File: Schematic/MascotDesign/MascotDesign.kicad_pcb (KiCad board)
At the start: 2 copper layers, 64 x 35.6 mm, 41 parts, among them J1 Charger input, J10 AudioJack4, J11 Main power cutoff (soldered s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, J2 PI power USB, J3 LCD LED Power, J5 Audio in, J6 Audio in, J8 Potentiometer, J9 Speaker 8R, U1 Generic_Buck_Regulator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

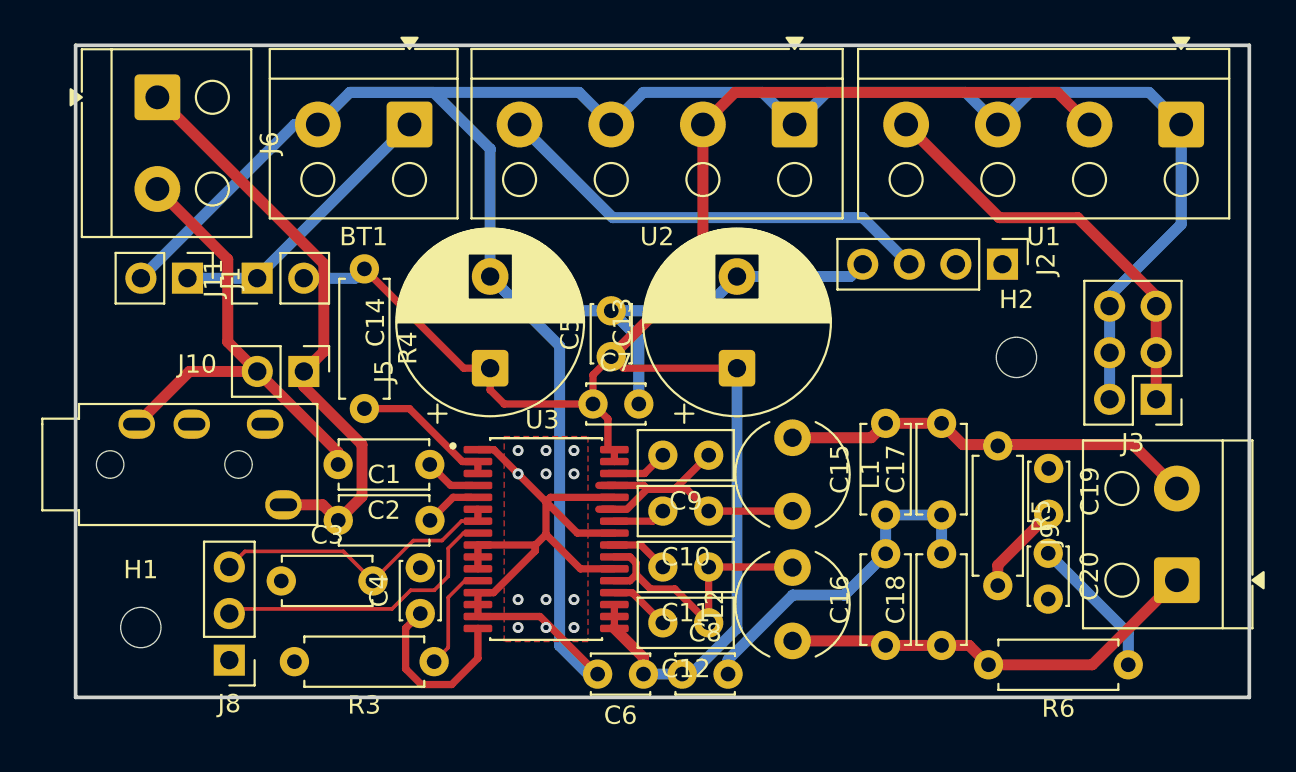
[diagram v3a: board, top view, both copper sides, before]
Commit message: ensure board passes DRC errors
not warnings though. Those are mostly just silkscreen overlaps.
We need to put something funny on the silkscreen yet.
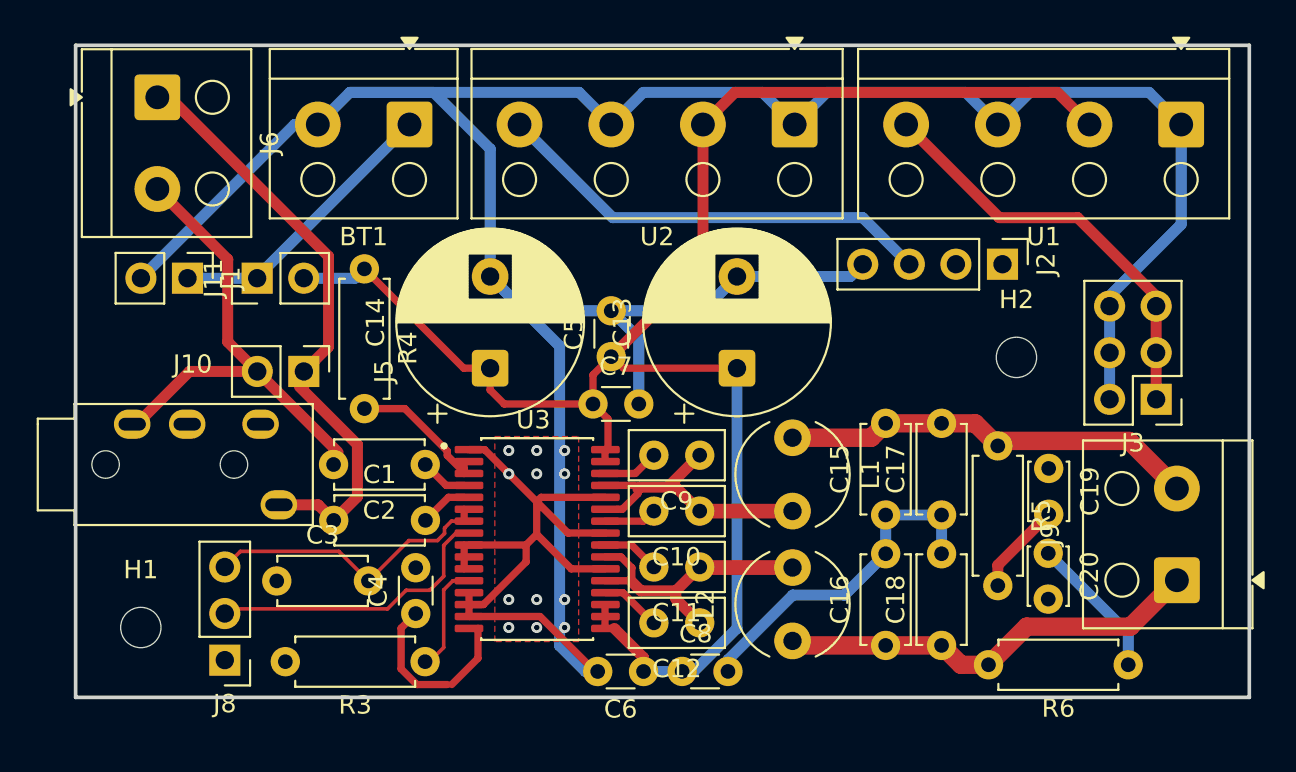
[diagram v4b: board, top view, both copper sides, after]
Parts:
- C4, C5, C6, C7, C8: footprint Capacitor_THT:C_Disc_D3.0mm_W2.0mm_P2.50mm -> Capacitor_THT:C_Disc_D3.0mm_W1.6mm_P2.50mm
- moved R3 0.49 mm to (96.3, 95.3)
- moved C10 0.49 mm to (111.3, 87.1)
- moved C11 0.49 mm to (111.3, 90.2)
- moved C12 0.49 mm to (111.3, 93.2)
- moved C9 0.49 mm to (111.3, 84.1)
- moved U3 0.49 mm to (102.4, 88.6)
- moved C1 0.25 mm to (91.3, 87.6)
- moved C2 0.25 mm to (96.3, 84.6)
- moved C3 0.25 mm to (88.2, 90.9)
- moved C4 0.25 mm to (95.8, 92.7)
- moved J10 0.25 mm to (75.2, 82.4)
- moved J8 0.25 mm to (85.4, 95.2)
- moved C8 0.15 mm to (110.3, 95.9)
- moved C6 0.14 mm to (108.2, 95.9)
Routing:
- net Net-(U3-OUTNR): track 18.0 -> 15.5 mm
- net GND: track 208.0 -> 209.0 mm
- net Net-(J5-Pin_1): track 32.5 -> 33.1 mm

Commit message: Tweak PCB and make power traces slightly thicker
They should be plenty wide for our application, but if we have room, we may as well.
I may go back and replace the speaker output traces with fill zones later to minimize impedance.
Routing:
- net 12V SWITCHED: track 95.1 -> 117.5 mm
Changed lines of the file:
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@@
 		(tags "Resistor Axial_DIN0207 series Axial Horizontal pin pitch 7.62mm 0.25W = 1/4W length 6.3mm diameter 2.5mm")
 		(property "Reference" "R4"
-			(at 4.318 -2.37 90)
+			(at 3.81 0 90)
 			(layer "F.SilkS")
 			(effects
@@
 		(tags "Inductor Radial series Radial pin pitch 4.00mm  diameter 6.0mm height 4.6mm")
 		(property "Reference" "L2"
-			(at 2 -4.758 90)
+			(at 2 0 90)
 			(layer "F.SilkS")
 			(effects
@@
 		(at 75.152 82.382)
 		(property "Reference" "J10"
-			(at 8.4455 -3.269 0)
+			(at 7.144 2.454 0)
 			(layer "F.SilkS")
 			(effects
@@
 		(tags "CP Radial series Radial pin pitch 5.00mm diameter 10mm height 16mm Electrolytic Capacitor")
 		(property "Reference" "C13"
-			(at 2.5 -6.25 90)
+			(at 1.605677 0 180)
 			(layer "F.SilkS")
 			(effects
@@
 		(tags "C Disc series Radial pin pitch 5.00mm diameter 4.7mm width 2.5mm Capacitor")
 		(property "Reference" "C17"
-			(at 2.5 -2.5 90)
+			(at 2.5 0 90)
 			(layer "F.SilkS")
 			(effects
@@
 		(tags "THT terminal block RND 205-00003 pitch 5mm size 20x9mm drill 1.3mm pad 2.5mm")
 		(property "Reference" "U1"
-			(at 7.5 -6.12 0)
+			(at 7.5 0 0)
 			(layer "F.SilkS")
 			(effects
@@
 		(tags "Through hole pin header THT 1x04 2.54mm single row")
 		(property "Reference" "J2"
-			(at 0 -2.38 90)
+			(at 0 -3.048 180)
 			(layer "F.SilkS")
 			(effects
@@
 		(tags "C Disc series Radial pin pitch 2.50mm diameter 3mm width 2mm Capacitor")
 		(property "Reference" "C20"
-			(at 1.25 -2.25 270)
+			(at 1.25 0 180)
 			(layer "F.SilkS")
 			(effects
@@
 		(tags "C Disc series Radial pin pitch 2.50mm diameter 3.0mm width 1.6mm Capacitor")
 		(property "Reference" "C4"
-			(at 1.25 -2.05 90)
+			(at 1.25 0 180)
 			(layer "F.SilkS")
 			(effects
@@
 		(tags "THT terminal block RND 205-00001 pitch 5mm size 10x9mm drill 1.3mm pad 2.5mm")
 		(property "Reference" "BT1"
-			(at 2.5 -6.12 0)
+			(at 2.5 -3.048 0)
 			(layer "F.SilkS")
 			(effects
@@
 		(tags "Resistor Axial_DIN0207 series Axial Horizontal pin pitch 7.62mm 0.25W = 1/4W length 6.3mm diameter 2.5mm")
 		(property "Reference" "R5"
-			(at 3.81 -2.37 90)
+			(at 3.81 0 90)
 			(layer "F.SilkS")
 			(effects
@@
 		(tags "C Disc series Radial pin pitch 5.00mm diameter 4.7mm width 2.5mm Capacitor")
 		(property "Reference" "C1"
-			(at 2.5 -2.5 0)
+			(at 2.5 0 0)
 			(layer "F.SilkS")
 			(effects
@@
 		(tags "Inductor Radial series Radial pin pitch 4.00mm  diameter 6.0mm height 4.6mm")
 		(property "Reference" "L1"
-			(at 2 -4.25 90)
+			(at 2 0 90)
 			(layer "F.SilkS")
 			(effects
@@
 		(tags "C Disc series Radial pin pitch 5.00mm diameter 4.7mm width 2.5mm Capacitor")
 		(property "Reference" "C3"
-			(at 2.5 -2.5 0)
+			(at 2.5 0 0)
 			(layer "F.SilkS")
 			(effects
@@
 		(tags "Resistor Axial_DIN0207 series Axial Horizontal pin pitch 7.62mm 0.25W = 1/4W length 6.3mm diameter 2.5mm")
 		(property "Reference" "R6"
-			(at 3.81 -2.37 0)
+			(at 3.81 0 0)
 			(layer "F.SilkS")
 			(effects
@@
 		)
 		(property "Value" "13.2 R"
-			(at 3.81 2.37 0)
+			(at 3.81 0 0)
 			(layer "F.Fab")
 			(effects
@@
 		(tags "C Disc series Radial pin pitch 2.50mm diameter 3.0mm width 1.6mm Capacitor")
 		(property "Reference" "C7"
-			(at 1.25 -2.05 0)
+			(at 1.25 0 90)
 			(layer "F.SilkS")
 			(effects
@@
 		(tags "C Disc series Radial pin pitch 2.50mm diameter 3.0mm width 1.6mm Capacitor")
 		(property "Reference" "C6"
-			(at 1.25 -2.05 180)
+			(at 4.555688 0 180)
 			(layer "F.SilkS")
 			(effects
@@
 		(tags "C Disc series Radial pin pitch 2.50mm diameter 3.0mm width 1.6mm Capacitor")
 		(property "Reference" "C5"
-			(at 1.25 -2.05 90)
+			(at 1.25 0 0)
 			(layer "F.SilkS")
 			(effects
@@
 		(tags "mountinghole M2")
 		(property "Reference" "H2"
-			(at 0 -3.15 0)
+			(at -3.556 0 0)
 			(layer "F.SilkS")
 			(effects
@@
 		(tags "C Disc series Radial pin pitch 2.50mm diameter 5mm width 2.5mm Capacitor")
 		(property "Reference" "C11"
-			(at 1.27 -2.5 180)
+			(at 1.25 0 270)
 			(layer "F.SilkS")
 			(effects
@@
 		(tags "Through hole pin header THT 1x03 2.54mm single row")
 		(property "Reference" "J8"
-			(at 0 -2.38 0)
+			(at 2.293 -0.762 0)
 			(layer "F.SilkS")
 			(effects
@@
 		(tags "Resistor Axial_DIN0207 series Axial Horizontal pin pitch 7.62mm 0.25W = 1/4W length 6.3mm diameter 2.5mm")
 		(property "Reference" "R3"
-			(at 3.81 -2.37 0)
+			(at 3.81 0 0)
 			(layer "F.SilkS")
 			(effects
@@
 		(tags "Through hole pin header THT 1x02 2.54mm single row")
 		(property "Reference" "J5"
-			(at 0 -4.372 90)
+			(at -0.005 5.08 180)
 			(layer "F.SilkS")
 			(effects
@@
 		(tags "C Disc series Radial pin pitch 2.50mm diameter 5mm width 2.5mm Capacitor")
 		(property "Reference" "C10"
-			(at 1.27 -2.5 180)
+			(at 1.25 0 270)
 			(layer "F.SilkS")
 			(effects
@@
 		(tags "C Disc series Radial pin pitch 5.00mm diameter 4.7mm width 2.5mm Capacitor")
 		(property "Reference" "C15"
-			(at 2.5 -2.5 90)
+			(at 2.5 0 90)
 			(layer "F.SilkS")
 			(effects
@@
 		(tags "THT terminal block RND 205-00003 pitch 5mm size 20x9mm drill 1.3mm pad 2.5mm")
 		(property "Reference" "U2"
-			(at 7.5 -6.12 0)
+			(at 7.5 0 0)
 			(layer "F.SilkS")
 			(effects
@@
 		(tags "CP Radial series Radial pin pitch 5.00mm diameter 10mm height 16mm Electrolytic Capacitor")
 		(property "Reference" "C14"
-			(at 2.5 -6.25 90)
+			(at 1.605677 0 180)
 			(layer "F.SilkS")
 			(effects
@@
 		(tags "Through hole pin header THT 1x02 2.54mm single row")
 		(property "Reference" "J11"
-			(at 0 -2.38 90)
+			(at -2.032 1.021 180)
 			(layer "F.SilkS")
 			(effects
@@
 		(tags "Through hole pin header THT 2x03 2.54mm double row")
 		(property "Reference" "J3"
-			(at 1.27 -2.38 0)
+			(at -2.794 0 90)
 			(layer "F.SilkS")
 			(effects
@@
 		(tags "C Disc series Radial pin pitch 2.50mm diameter 3mm width 2mm Capacitor")
 		(property "Reference" "C19"
-			(at 1.25 -2.25 270)
+			(at -2.499928 -0.019748 270)
 			(layer "F.SilkS")
 			(effects
@@
 		(tags "THT terminal block RND 205-00001 pitch 5mm size 10x9mm drill 1.3mm pad 2.5mm")
 		(property "Reference" "J9"
-			(at 2.5 -6.902 90)
+			(at 2.5 0.1405 180)
 			(layer "F.SilkS")
 			(effects
@@
 		(tags "C Disc series Radial pin pitch 2.50mm diameter 5mm width 2.5mm Capacitor")
 		(property "Reference" "C12"
-			(at 1.25 -2.5 180)
+			(at 1.25 0 270)
 			(layer "F.SilkS")
 			(effects
@@
 		)
 		(property "Value" "1 uF"
-			(at 2.5 2.5 90)
+			(at 2.5 1.036 90)
 			(layer "F.Fab")
 			(effects
@@
 		(tags "C Disc series Radial pin pitch 5.00mm diameter 4.7mm width 2.5mm Capacitor")
 		(property "Reference" "C2"
-			(at 2.5 -2.5 180)
+			(at 2.490445 0 180)
 			(layer "F.SilkS")
 			(effects
@@
 		(tags "Through hole pin header THT 1x02 2.54mm single row")
 		(property "Reference" "J1"
-			(at 0 -2.38 90)
+			(at 2.54 1.275 180)
 			(layer "F.SilkS")
 			(effects
@@
 		(tags "THT terminal block RND 205-00001 pitch 5mm size 10x9mm drill 1.3mm pad 2.5mm")
 		(property "Reference" "J6"
-			(at 2.5 -6.12 90)
+			(at 2.5 0.1405 0)
 			(layer "F.SilkS")
 			(effects
@@
 		(tags "C Disc series Radial pin pitch 2.50mm diameter 5mm width 2.5mm Capacitor")
 		(property "Reference" "C9"
-			(at 1.27 -2.5 180)
+			(at 1.25 0 270)
 			(layer "F.SilkS")
 			(effects
@@
 		(tags "C Disc series Radial pin pitch 2.50mm diameter 3.0mm width 1.6mm Capacitor")
 		(property "Reference" "C8"
-			(at 0.742 -2.05 0)
+			(at 4.516389 0 0)
 			(layer "F.SilkS")
 			(effects
@@
 	)
 	(segment
+		(start 132.508 65.706)
+		(end 132.508 66.04)
+		(width 1)
+		(layer "F.Cu")
+		(net 5)
+	)
+	(segment
 		(start 105.43 81.28)
 		(end 105.43 79.696)
@@
 	)
 	(segment
+		(start 130.556 63.754)
+		(end 132.508 65.706)
+		(width 1)
+		(layer "F.Cu")
+		(net 5)
+	)
+	(segment
+		(start 109.475 67.991)
+		(end 98.887 67.991)
+		(width 1)
+		(layer "F.Cu")
+		(net 5)
+	)
+	(segment
 		(start 108.184 95.109)
 		(end 106.596 93.521)
@@
 	)
 	(segment
+		(start 98.887 67.991)
+		(end 92.964 73.914)
+		(width 1)
+		(layer "F.Cu")
+		(net 5)
+	)
+	(segment
 		(start 105.43 79.696)
 		(end 106.426 78.7)
@@
 	)
 	(segment
+		(start 111.426 66.04)
+		(end 109.475 67.991)
+		(width 1)
+		(layer "F.Cu")
+		(net 5)
+	)
+	(segment
 		(start 111.426 73.7)
 		(end 106.426 78.7)
@@
 	)
 	(segment
-		(start 106.088 93.521)
-		(end 106.088 92.221)
-		(width 0.4)
-		(layer "F.Cu")
-		(net 5)
-	)
-	(segment
-		(start 130.757 64.289)
-		(end 132.508 66.04)
-		(width 0.6)
+		(start 111.426 66.04)
+		(end 113.712 63.754)
+		(width 1)
 		(layer "F.Cu")
 		(net 5)
 	)
 	(segment
-		(start 113.177 64.289)
-		(end 130.757 64.289)
-		(width 0.6)
+		(start 106.088 93.521)
+		(end 106.088 92.221)
+		(width 0.4)
 		(layer "F.Cu")
 		(net 5)
@@
 	)
 	(segment
-		(start 111.426 66.04)
-		(end 113.177 64.289)
-		(width 0.6)
+		(start 113.712 63.754)
+		(end 130.556 63.754)
+		(width 1)
 		(layer "F.Cu")
 		(net 5)
@@
 		(start 92.456 74.422)
 		(end 92.964 73.914)
-		(width 0.6)
+		(width 1)
 		(layer "B.Cu")
 		(net 5)
@@
 		(start 89.657 74.422)
 		(end 92.456 74.422)
-		(width 0.6)
+		(width 1)
 		(layer "B.Cu")
 		(net 5)
@@
 		(start 95.424 66.04)
 		(end 87.117 74.347)
-		(width 0.6)
+		(width 1)
 		(layer "B.Cu")
 		(net 18)
@@
 		(start 86.863 74.422)
 		(end 83.317 74.422)
-		(width 0.6)
+		(width 1)
 		(layer "B.Cu")
 		(net 18)
@@
 		(start 87.117 74.347)
 		(end 87.117 74.422)
-		(width 0.6)
+		(width 1)
 		(layer "B.Cu")
 		(net 18)
@@
 			)
 		)
+	)
+	(zone
+		(net 0)
+		(net_name "")
+		(layer "F.Mask")
+		(hatch edge 0.5)
+		(connect_pads
+			(clearance 0.5)
+		)
+		(min_thickness 0.25)
+		(filled_areas_thickness no)
+		(fill yes
+			(thermal_gap 0.5)
+			(thermal_bridge_width 0.5)
+		)
+		(polygon
+			(pts
+				(xy 104.648 83.058) (xy 100.076 83.058) (xy 100.076 94.234) (xy 104.648 94.234)
+			)
+		)

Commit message: Add screen mounts to CAD and PCB silkscreen
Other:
- board text added: "JLCJLCJLCJLC"
- board text added: "Mascot Head Terminal board Rev. 1.0"

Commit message: Slight PCB tweaking
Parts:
- J1: footprint Connector_PinHeader_2.54mm:PinHeader_1x02_P2.54mm_Vertical -> Connector_JST:JST_XH_B2B-XH-A_1x02_P2.50mm_Vertical
- J3: footprint Connector_PinHeader_2.54mm:PinHeader_2x03_P2.54mm_Vertical -> Connector_PinHeader_2.54mm:PinHeader_2x04_P2.54mm_Vertical
- moved J3 7.65 mm to (135.2, 73.4), turned to 0 degrees
- moved J1 4.51 mm to (80.8, 78.2), turned to 90 degrees
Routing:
- net +12V: track 15.4 -> 19.5 mm
- net Net-(J9-Pin_2): track 23.0 -> 24.3 mm
- net GND: track 209.0 -> 208.0 mm, vias 12 -> 18
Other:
- board text added: "github.com/DrGlaucous/mascot-head-sr-design"

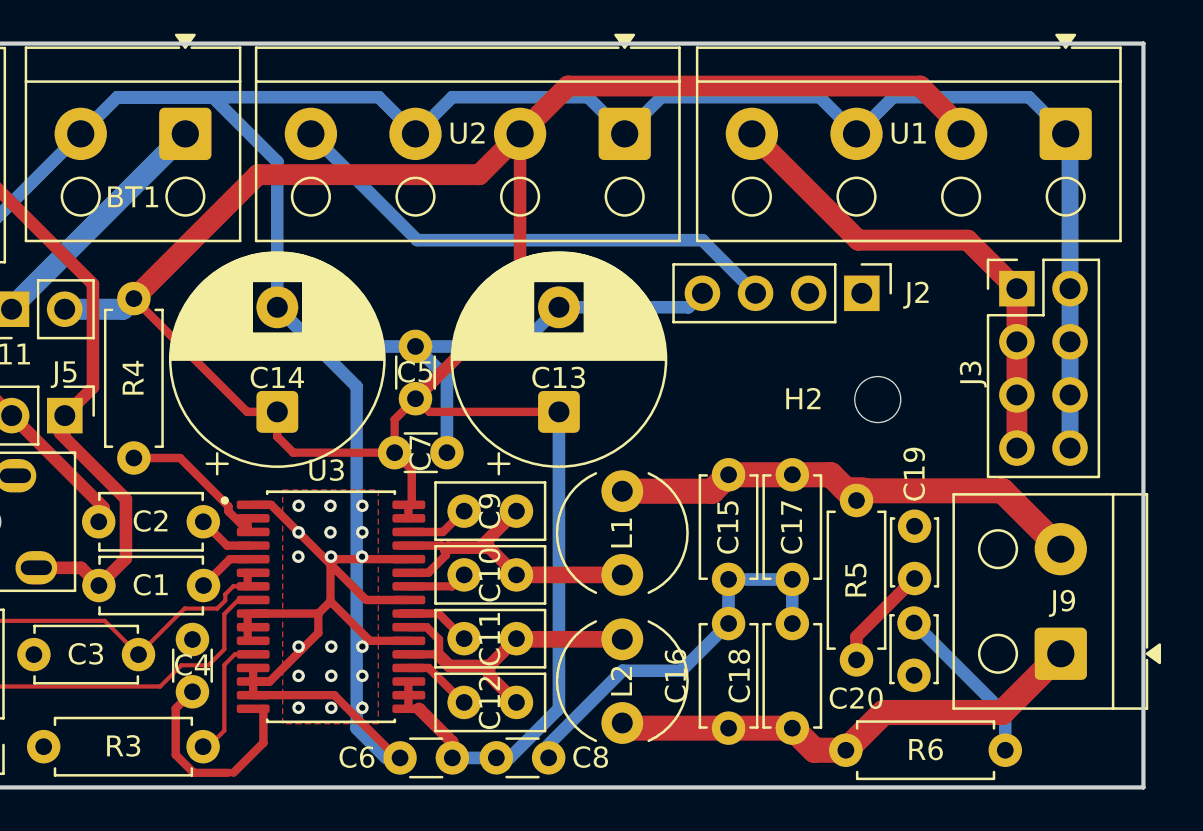
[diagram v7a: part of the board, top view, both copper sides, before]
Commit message: Finalize and order PCB
Ordered through JLC, so formatting was exported to match that
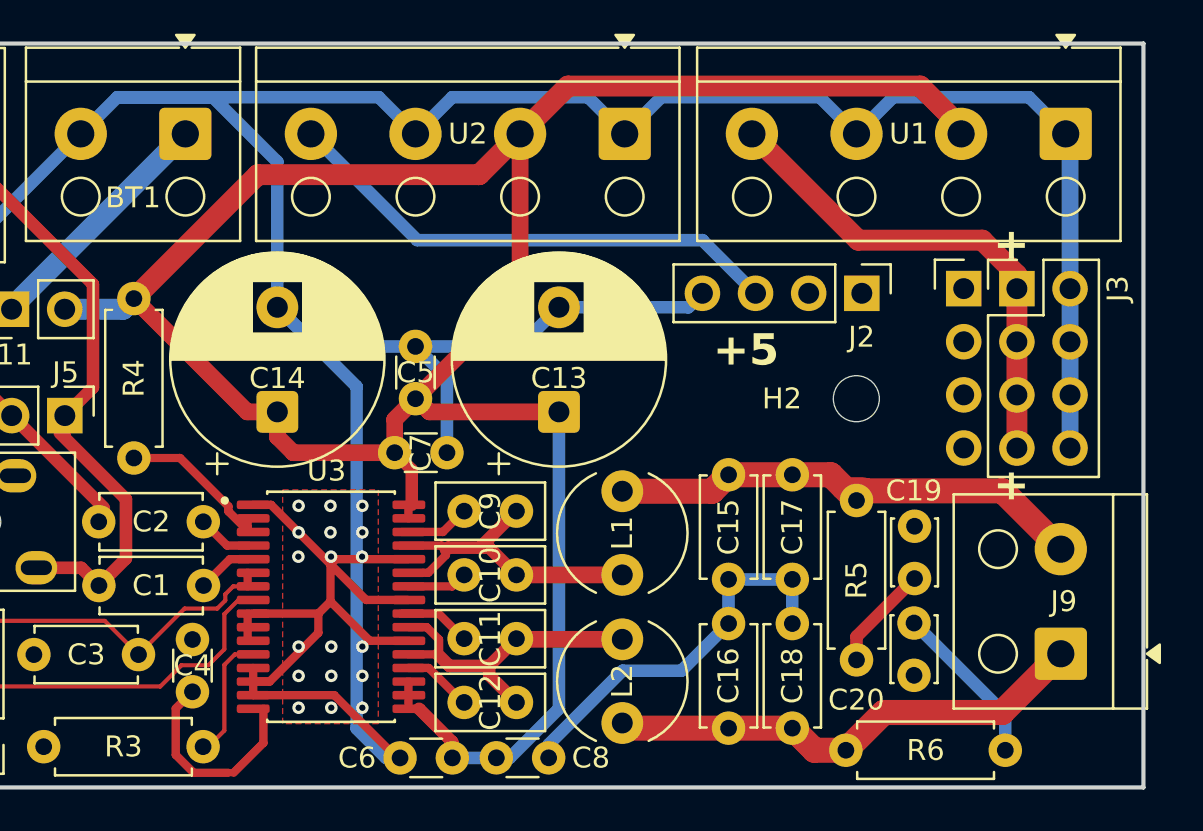
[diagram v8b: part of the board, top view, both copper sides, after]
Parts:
- added J4: Dummy Header, Connector_PinHeader_2.54mm:PinHeader_1x04_P2.54mm_Vertical, F.Cu at (132.6, 73.4)
- moved H2 1.02 mm to (127.5, 78.7)
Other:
- board text added: "+"
- board text added: "+12"
- board text added: "+5"
- board text added: "Audio"
- board text added: "SP"
